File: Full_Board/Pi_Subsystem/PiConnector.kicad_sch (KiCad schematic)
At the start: 4 parts

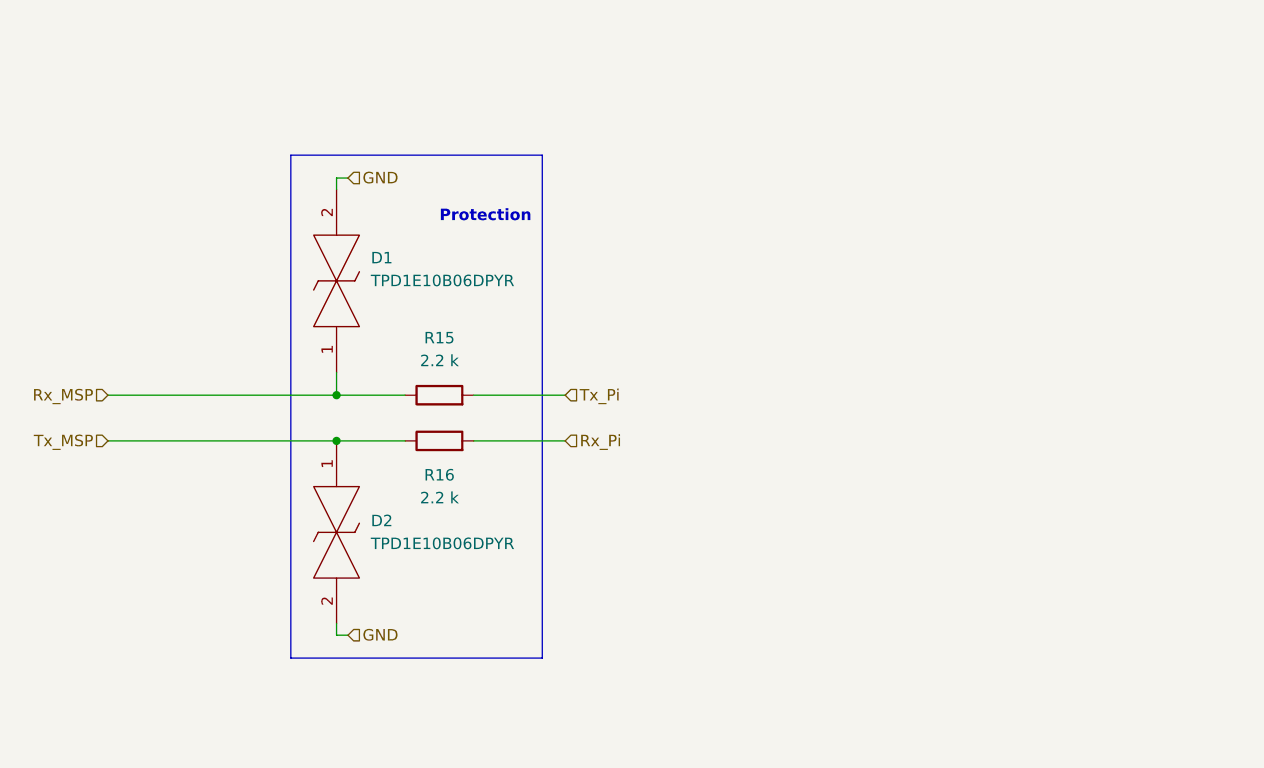
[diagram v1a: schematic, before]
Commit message: Swapped TVS Diodes
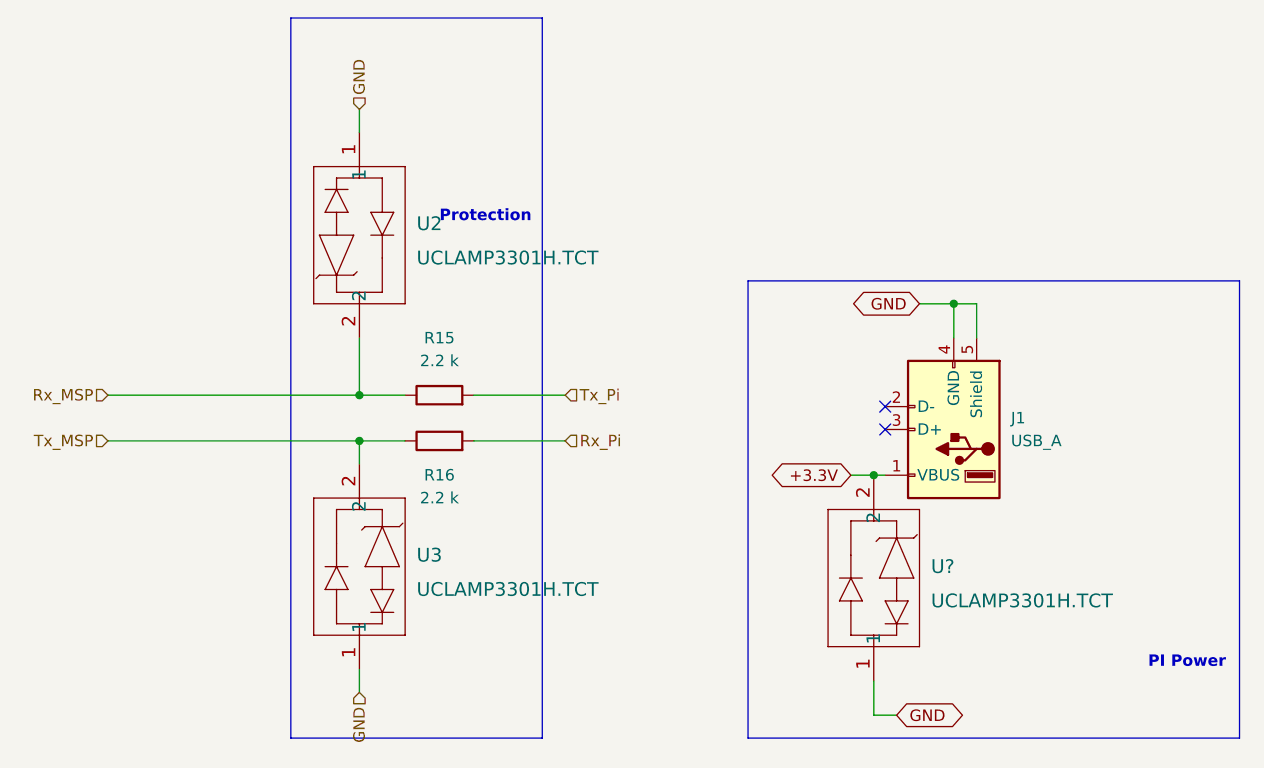
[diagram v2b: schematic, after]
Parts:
- removed D1, D2: TPD1E10B06DPYR, TPD1E10B06DPYR:TPD1E10B06DPYR, symbol TPD1E10B06DPYR:TPD1E10B06DPYR
- added J1: USB_A, USB1130-15-A:USB1130-15-A, symbol Connector:USB_A
- added U2, U3, U?: UCLAMP3301H.TCT, SOD_01H.TCT_SEM, symbol UCLAMP3301H-TCT:UCLAMP3301H.TCT
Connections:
- net GND: now also J1.4 (GND), J1.5 (Shield), U2.1, U3.1, U?.1
- net Rx_MSP: now also U2.2
- net Tx_MSP: now also U3.2
- new net +3.3V: J1.1 (VBUS), U?.2
- no-connect marks 0 -> 2
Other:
- note added: "PI Power"

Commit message: Relayed out the power supply and stepper drivers
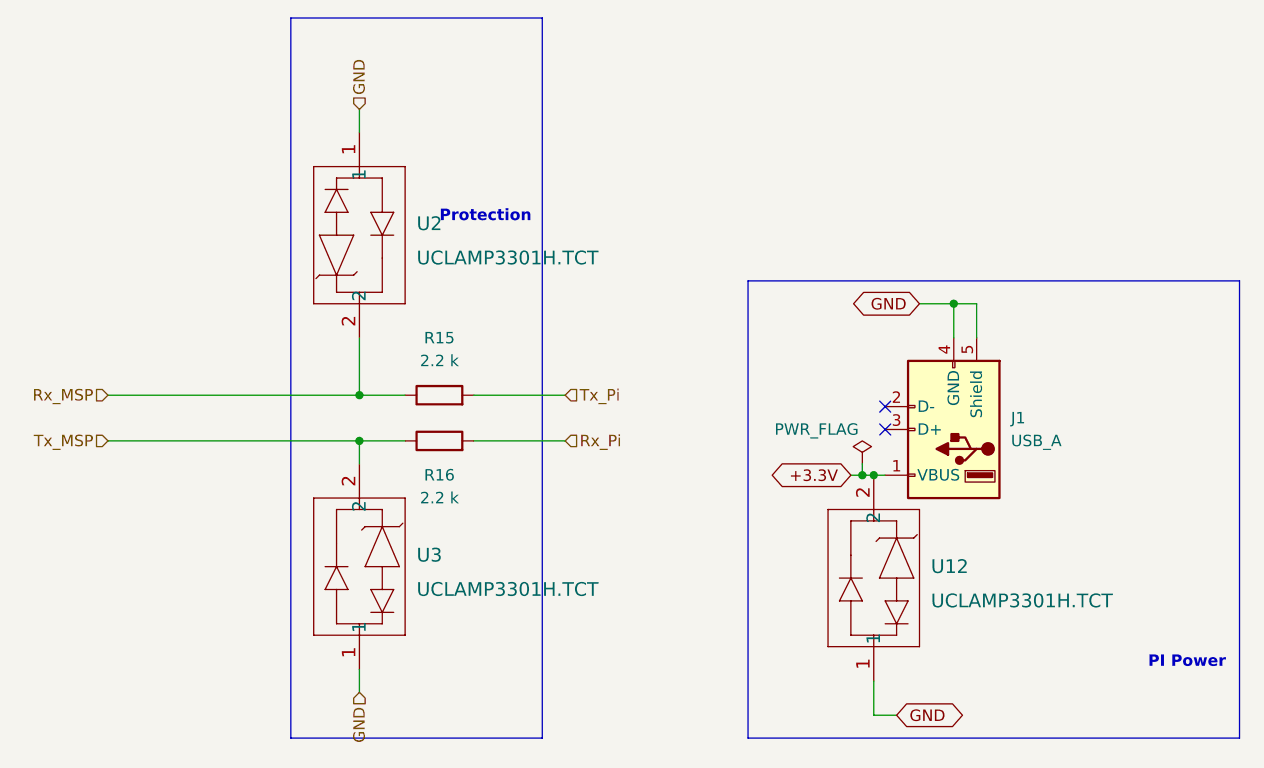
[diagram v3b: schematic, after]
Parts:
- U12: renamed from U?; footprint SOD_01H.TCT_SEM -> UCLAMP3310H-TCT:UCLAMP3301H.TCT
- U2, U3: footprint SOD_01H.TCT_SEM -> UCLAMP3310H-TCT:UCLAMP3301H.TCT
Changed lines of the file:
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@@
   (junction (at 220.98 87.63) (diameter 0) (color 0 0 0 0)
+  )
+  (junction (at 210.82 106.68) (diameter 0) (color 0 0 0 0)
   )
   (junction (at 154.94 97.79) (diameter 0) (color 0 0 0 0)
@@
     (stroke (width 0) (type default) (color 0 0 0 0))
   )
+  (wire (pts (xy 210.82 105.41) (xy 210.82 106.68))
+    (stroke (width 0) (type default) (color 0 0 0 0))
+  )
   (wire (pts (xy 167.64 97.79) (xy 177.8 97.79))
     (stroke (width 0) (type default) (color 0 0 0 0))
   )
+  (wire (pts (xy 210.82 106.68) (xy 212.09 106.68))
+    (stroke (width 0) (type default) (color 0 0 0 0))
+  )
   (wire (pts (xy 154.94 102.87) (xy 160.02 102.87))
     (stroke (width 0) (type default) (color 0 0 0 0))
@@
     (stroke (width 0) (type default) (color 0 0 0 0))
   )
-  (wire (pts (xy 209.55 106.68) (xy 212.09 106.68))
+  (wire (pts (xy 209.55 106.68) (xy 210.82 106.68))
     (stroke (width 0) (type default) (color 0 0 0 0))
   )
@@
       (effects (font (size 1.524 1.524)) (justify left))
     )
-    (property "Footprint" "SOD_01H.TCT_SEM" (id 2) (at 170.18 82.55 0)
+    (property "Footprint" "UCLAMP3310H-TCT:UCLAMP3301H.TCT" (id 2) (at 170.18 82.55 0)
       (effects (font (size 1.524 1.524)) hide)
     )
@@
     (pin "2")
   )
-  (symbol (lib_id "UCLAMP3301H-TCT:UCLAMP3301H.TCT") (at 212.09 138.43 90) (unit 1)
-    (in_bom yes) (on_board yes) (fields_autoplaced)
-    (property "Reference" "U?" (id 0) (at 218.44 116.84 90)
+  (symbol (lib_name "UCLAMP3301H.TCT_1") (lib_id "UCLAMP3301H-TCT:UCLAMP3301H.TCT") (at 212.09 138.43 90) (unit 1)
+    (in_bom yes) (on_board yes) (fields_autoplaced)
+    (property "Reference" "U12" (id 0) (at 218.44 116.84 90)
       (effects (font (size 1.524 1.524)) (justify right))
     )
@@
       (effects (font (size 1.524 1.524)) (justify right))
     )
-    (property "Footprint" "SOD_01H.TCT_SEM" (id 2) (at 196.85 115.57 0)
+    (property "Footprint" "UCLAMP3310H-TCT:UCLAMP3301H.TCT" (id 2) (at 196.85 115.57 0)
       (effects (font (size 1.524 1.524)) hide)
     )
@@
     (pin "2")
   )
-  (symbol (lib_id "UCLAMP3301H-TCT:UCLAMP3301H.TCT") (at 154.94 137.16 90) (unit 1)
+  (symbol (lib_name "UCLAMP3301H.TCT_2") (lib_id "UCLAMP3301H-TCT:UCLAMP3301H.TCT") (at 154.94 137.16 90) (unit 1)
     (in_bom yes) (on_board yes) (fields_autoplaced)
     (property "Reference" "U3" (id 0) (at 161.29 115.57 90)
@@
       (effects (font (size 1.524 1.524)) (justify right))
     )
-    (property "Footprint" "SOD_01H.TCT_SEM" (id 2) (at 139.7 114.3 0)
+    (property "Footprint" "UCLAMP3310H-TCT:UCLAMP3301H.TCT" (id 2) (at 139.7 114.3 0)
       (effects (font (size 1.524 1.524)) hide)
     )
@@
     (pin "2")
   )
+  (symbol (lib_id "power:PWR_FLAG") (at 210.82 105.41 0) (unit 1)
+    (in_bom yes) (on_board yes)
+    (property "Reference" "#FLG0101" (id 0) (at 210.82 103.505 0)
+      (effects (font (size 1.27 1.27)) hide)
+    )
+    (property "Value" "PWR_FLAG" (id 1) (at 205.74 101.6 0))
+    (property "Footprint" "" (id 2) (at 210.82 105.41 0)
+      (effects (font (size 1.27 1.27)) hide)
+    )
+    (property "Datasheet" "~" (id 3) (at 210.82 105.41 0)
+      (effects (font (size 1.27 1.27)) hide)
+    )
+    (pin "1")
+  )
 )

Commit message: More layout work
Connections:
- net +3.3V renamed 5V
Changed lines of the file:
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@@
     (stroke (width 0) (type default) (color 0 0 0 0))
   )
-  (wire (pts (xy 212.09 133.35) (xy 214.63 133.35))
+  (wire (pts (xy 212.09 133.35) (xy 215.9 133.35))
     (stroke (width 0) (type default) (color 0 0 0 0))
   )
@@
     (stroke (width 0) (type default) (color 0 0 0 0))
   )
-  (wire (pts (xy 209.55 106.68) (xy 210.82 106.68))
+  (wire (pts (xy 207.01 106.68) (xy 210.82 106.68))
     (stroke (width 0) (type default) (color 0 0 0 0))
   )
@@
     (stroke (width 0) (type default) (color 0 0 0 0))
   )
-  (wire (pts (xy 220.98 87.63) (xy 217.17 87.63))
+  (wire (pts (xy 214.63 87.63) (xy 220.98 87.63))
     (stroke (width 0) (type default) (color 0 0 0 0))
   )
@@
     (effects (font (size 1.27 1.27) (thickness 0.254) bold) (justify left bottom))
   )
-  (global_label "+3.3V" (shape bidirectional) (at 209.55 106.68 180) (fields_autoplaced)
+  (hierarchical_label "GND" (shape input) (at 214.63 87.63 180)
     (effects (font (size 1.27 1.27)) (justify right))
-    (property "Intersheet References" "${INTERSHEET_REFS}" (id 0) (at 201.4521 106.7594 0)
-      (effects (font (size 1.27 1.27)) (justify right) hide)
-    )
   )
-  (global_label "GND" (shape bidirectional) (at 214.63 133.35 0) (fields_autoplaced)
+  (hierarchical_label "GND" (shape input) (at 215.9 133.35 0)
     (effects (font (size 1.27 1.27)) (justify left))
-    (property "Intersheet References" "${INTERSHEET_REFS}" (id 0) (at 220.9136 133.2706 0)
-      (effects (font (size 1.27 1.27)) (justify left) hide)
-    )
   )
-  (global_label "GND" (shape bidirectional) (at 217.17 87.63 180) (fields_autoplaced)
+  (hierarchical_label "5V" (shape input) (at 207.01 106.68 180)
     (effects (font (size 1.27 1.27)) (justify right))
-    (property "Intersheet References" "${INTERSHEET_REFS}" (id 0) (at 210.8864 87.7094 0)
-      (effects (font (size 1.27 1.27)) (justify right) hide)
-    )
   )
   (hierarchical_label "GND" (shape input) (at 154.94 130.81 270)

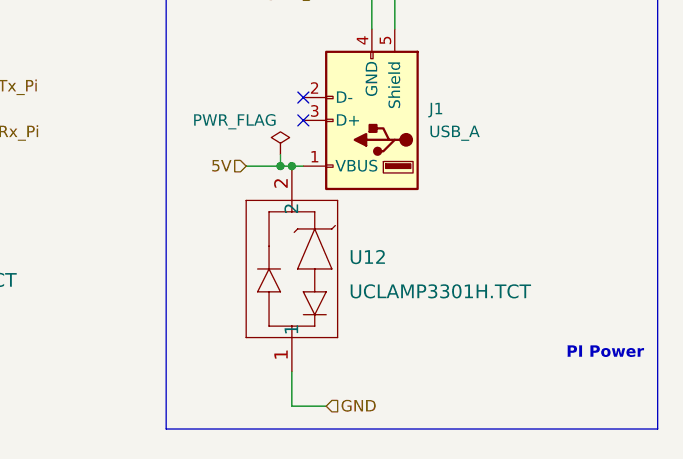
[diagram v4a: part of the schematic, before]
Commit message: Layed out stepper connectors and test points
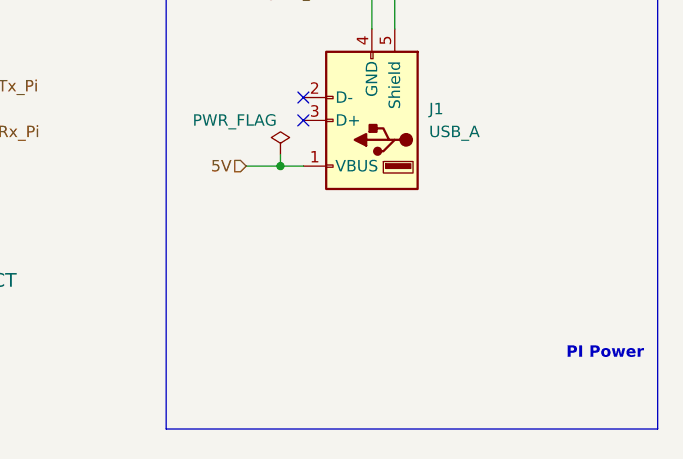
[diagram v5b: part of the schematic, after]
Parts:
- removed U12: UCLAMP3301H.TCT, UCLAMP3310H-TCT:UCLAMP3301H.TCT, symbol UCLAMP3301H-TCT:UCLAMP3301H.TCT
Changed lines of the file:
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@@
     (company "The Great Gambit")
-  )
-  (junction (at 212.09 106.68) (diameter 0) (color 0 0 0 0)
   )
   (junction (at 154.94 102.87) (diameter 0) (color 0 0 0 0)
@@
     (stroke (width 0) (type default) (color 0 0 0 0))
   )
-  (wire (pts (xy 212.09 133.35) (xy 215.9 133.35))
-    (stroke (width 0) (type default) (color 0 0 0 0))
-  )
   (wire (pts (xy 223.52 87.63) (xy 220.98 87.63))
     (stroke (width 0) (type default) (color 0 0 0 0))
@@
     (stroke (width 0) (type default) (color 0 0 0 0))
   )
-  (wire (pts (xy 212.09 129.54) (xy 212.09 133.35))
-    (stroke (width 0) (type default) (color 0 0 0 0))
-  )
   (wire (pts (xy 154.94 91.44) (xy 154.94 97.79))
     (stroke (width 0) (type default) (color 0 0 0 0))
@@
     (stroke (width 0) (type default) (color 0 0 0 0))
   )
-  (wire (pts (xy 210.82 106.68) (xy 212.09 106.68))
+  (wire (pts (xy 210.82 106.68) (xy 213.36 106.68))
     (stroke (width 0) (type default) (color 0 0 0 0))
   )
@@
   )
   (polyline (pts (xy 252.73 135.89) (xy 198.12 135.89))
-    (stroke (width 0) (type default) (color 0 0 0 0))
-  )
-  (wire (pts (xy 212.09 106.68) (xy 213.36 106.68))
     (stroke (width 0) (type default) (color 0 0 0 0))
   )
@@
   (hierarchical_label "GND" (shape input) (at 214.63 87.63 180)
     (effects (font (size 1.27 1.27)) (justify right))
-  )
-  (hierarchical_label "GND" (shape input) (at 215.9 133.35 0)
-    (effects (font (size 1.27 1.27)) (justify left))
   )
   (hierarchical_label "5V" (shape input) (at 207.01 106.68 180)
@@
       (effects (font (size 1.27 1.27)) hide)
     )
-    (pin "1")
-    (pin "2")
-  )
-  (symbol (lib_name "UCLAMP3301H.TCT_1") (lib_id "UCLAMP3301H-TCT:UCLAMP3301H.TCT") (at 212.09 138.43 90) (unit 1)
-    (in_bom yes) (on_board yes) (fields_autoplaced)
-    (property "Reference" "U12" (id 0) (at 218.44 116.84 90)
-      (effects (font (size 1.524 1.524)) (justify right))
-    )
-    (property "Value" "UCLAMP3301H.TCT" (id 1) (at 218.44 120.65 90)
-      (effects (font (size 1.524 1.524)) (justify right))
-    )
-    (property "Footprint" "UCLAMP3310H-TCT:UCLAMP3301H.TCT" (id 2) (at 196.85 115.57 0)
-      (effects (font (size 1.524 1.524)) hide)
-    )
-    (property "Datasheet" "https://semtech.my.salesforce.com/sfc/p/#E0000000JelG/a/44000000MDWf/s0KJxyOHQyYOcvBXVBK9X3X8Cxj1gNltZ2vd2k1S0Wo" (id 3) (at 220.98 137.16 0)
-      (effects (font (size 1.524 1.524)) hide)
-    )
-    (property "Manufacturers Part Number" "UCLAMP3301H.TCT" (id 4) (at 198.12 134.62 0)
-      (effects (font (size 1.27 1.27)) hide)
-    )
-    (property "Digikey Part Number" "UCLAMP3301HDKR-ND" (id 5) (at 200.66 135.89 0)
-      (effects (font (size 1.27 1.27)) hide)
-    )
-    (property "Mouser Part Number" "" (id 6) (at 212.09 138.43 0)
-      (effects (font (size 1.27 1.27)) hide)
-    )
-    (property "Digikey Link" "https://www.digikey.com/en/products/detail/semtech-corporation/UCLAMP3301H-TCT/1000952" (id 7) (at 220.98 137.16 0)
-      (effects (font (size 1.27 1.27)) hide)
-    )
-    (property "Mouser Link" "" (id 8) (at 212.09 138.43 0)
-      (effects (font (size 1.27 1.27)) hide)
-    )
